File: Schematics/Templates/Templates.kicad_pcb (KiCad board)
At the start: 4 copper layers, 69.5 x 60 mm, 0 parts

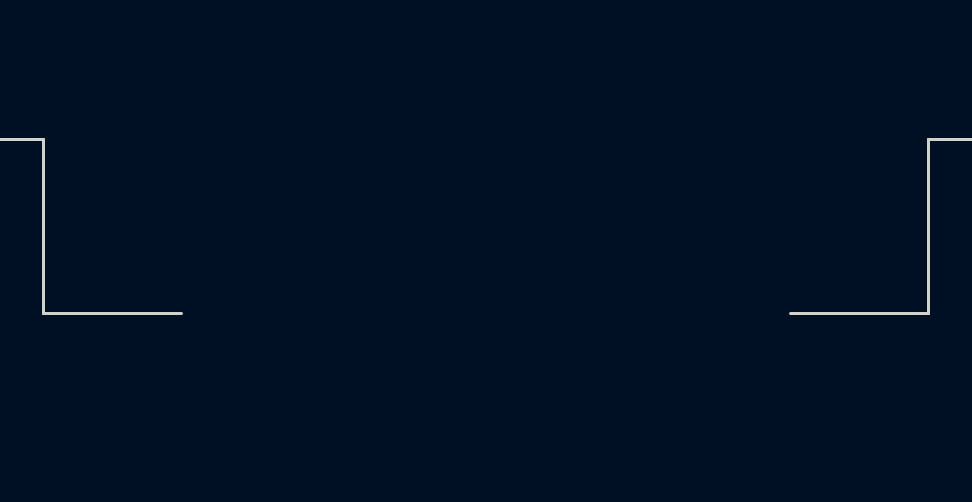
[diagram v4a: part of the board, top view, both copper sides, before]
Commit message: Increased available space at front of PCB
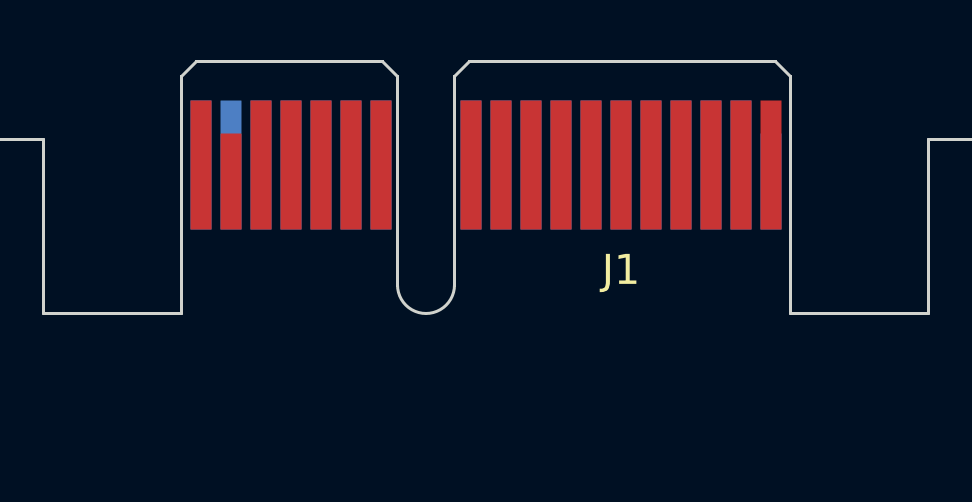
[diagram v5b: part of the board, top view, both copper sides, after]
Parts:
- added J1: Stack Male Edge Connector, Connector_PCBEdge:BUS_PCIexpress_x1, F.Cu at (66.4, 21.0)
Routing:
- added copper zone on In1.Cu, net Net-(J1-GND_B-PadA12)
- added copper zone on In2.Cu, net Net-(J1-GND_B-PadA12)
- removed copper zone on In1.Cu, net GND
- removed copper zone on In2.Cu, net GND

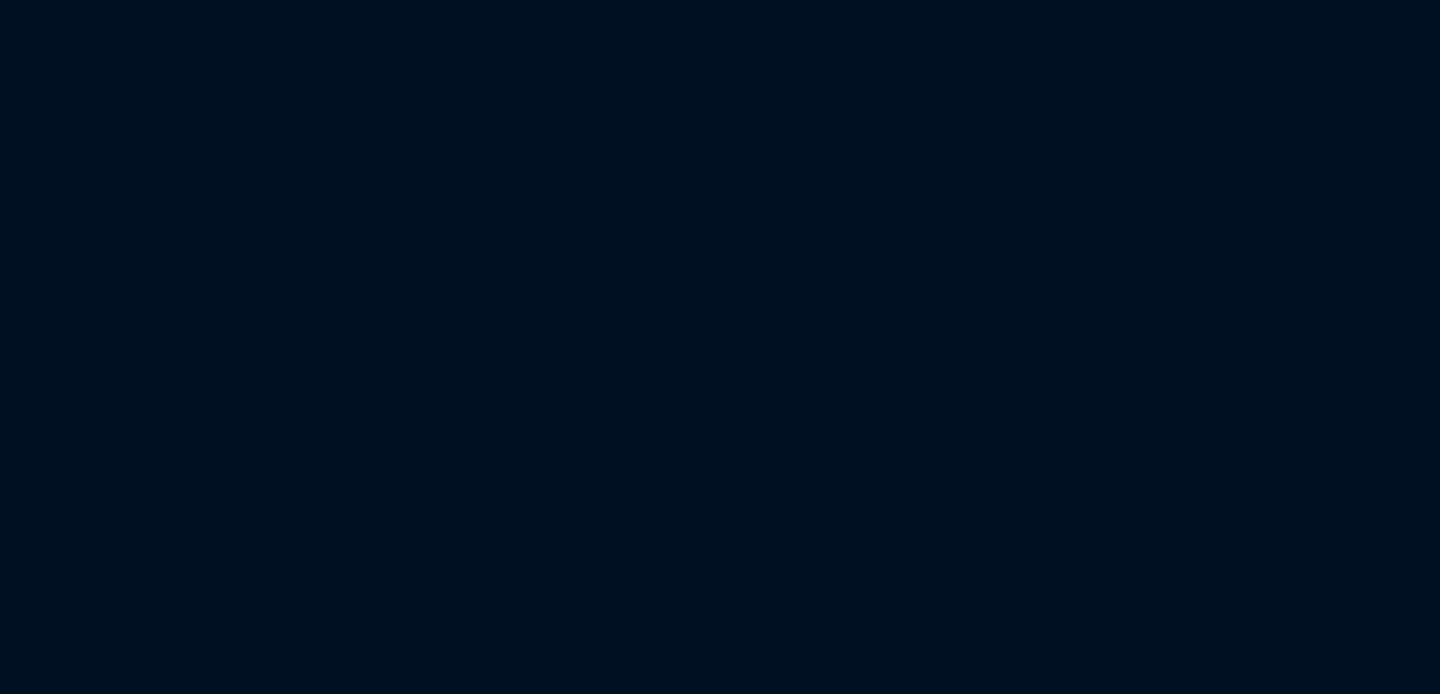
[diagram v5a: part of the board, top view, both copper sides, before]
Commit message: Add side silkscreen templates
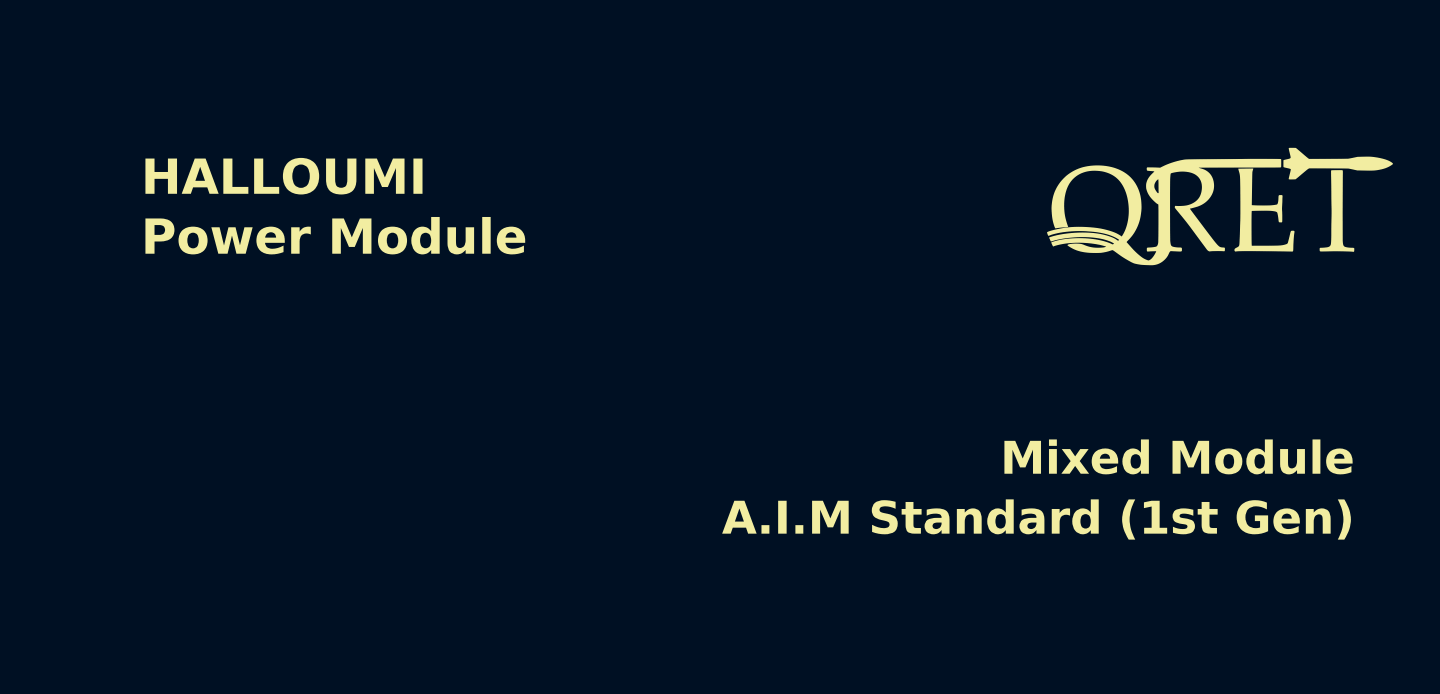
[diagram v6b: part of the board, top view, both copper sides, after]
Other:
- board text added: "A.I.M Standard (1st Gen)"
- board text added: "HALLOUMI"
- board text added: "Mixed Module"
- board text added: "Power Module"
